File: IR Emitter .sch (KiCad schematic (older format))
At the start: 19 parts, among them U11 ULN2003APWR, U12 SMT_0540-S-R

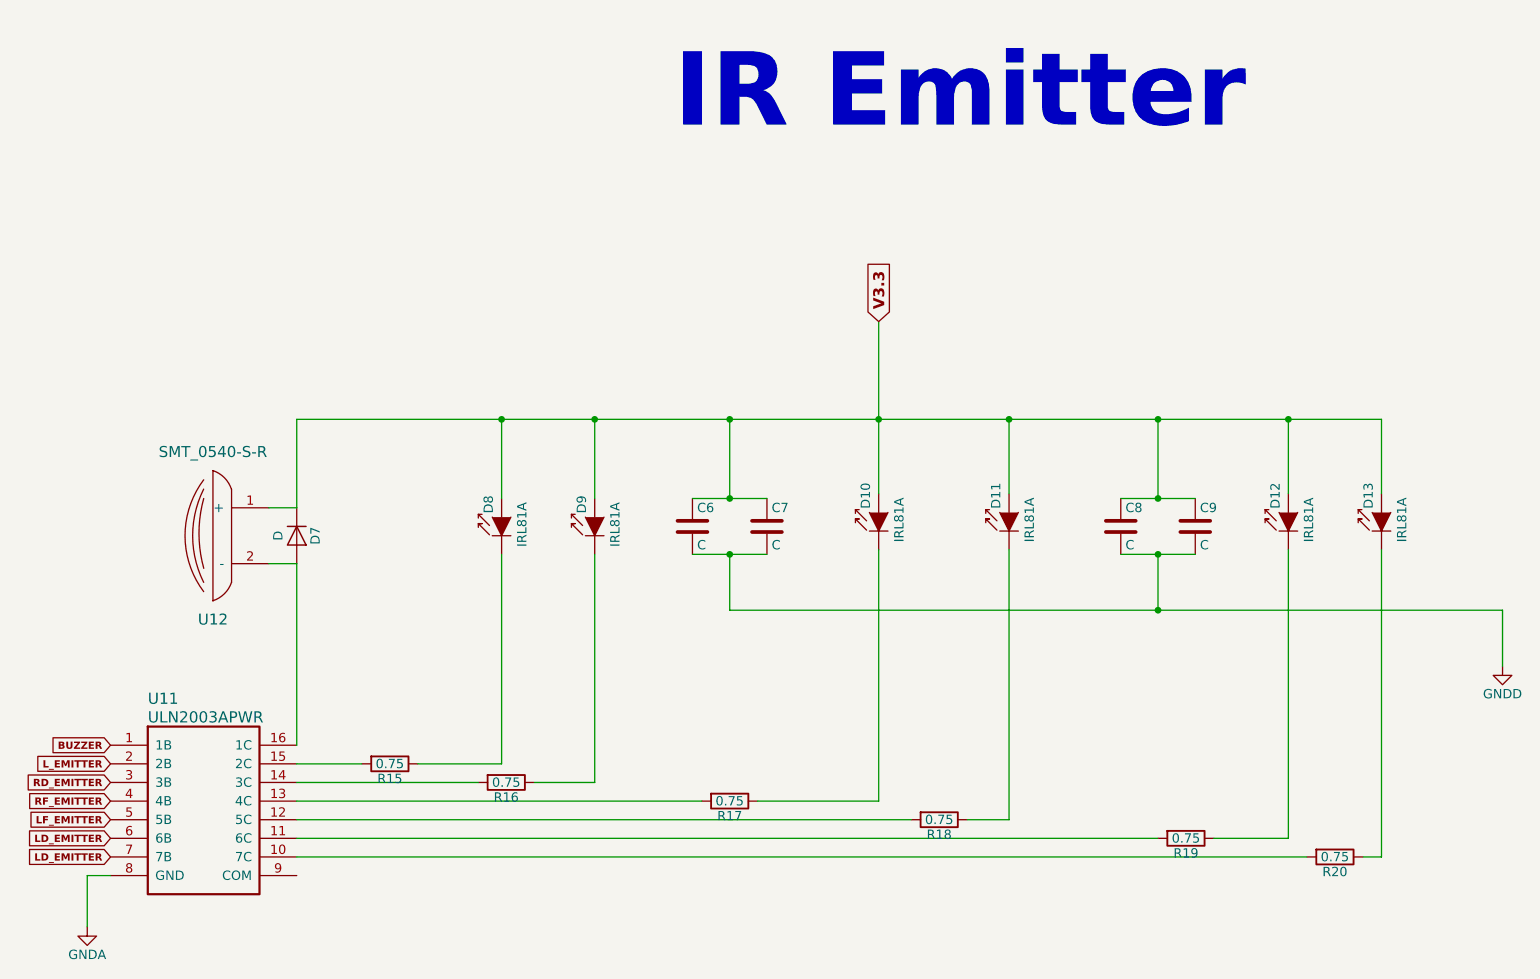
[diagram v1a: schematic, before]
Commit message: fixed the mergre conflicts from the adding datasheet commite
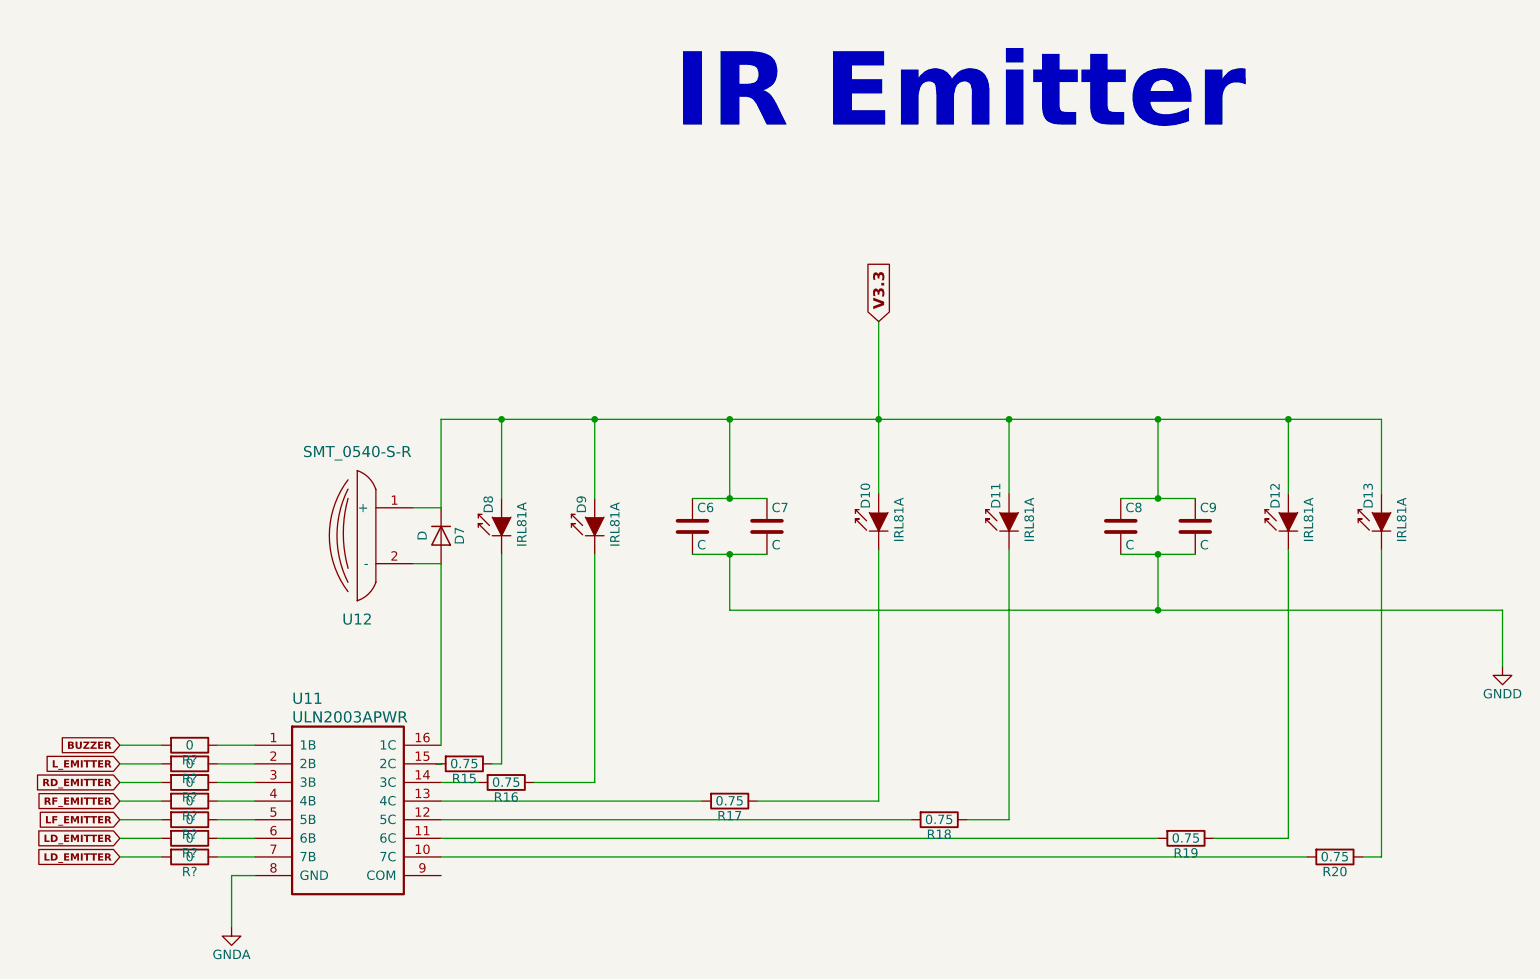
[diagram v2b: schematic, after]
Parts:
- added R? (x7): 0, symbol R
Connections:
- net BUZZER: now also R?.2; no longer U11.1 (1B)
- net LD_EMITTER: now also R?.2, R?.2; no longer U11.6 (6B), U11.7 (7B)
- net LF_EMITTER: now also R?.2; no longer U11.5 (5B)
- net L_EMITTER: now also R?.2; no longer U11.2 (2B)
- net RD_EMITTER: now also R?.2; no longer U11.3 (3B)
- net RF_EMITTER: now also R?.2; no longer U11.4 (4B)
- new net: R?.1, U11.1 (1B)
- new net: R?.1, U11.2 (2B)
- new net: R?.1, U11.3 (3B)
- new net: R?.1, U11.4 (4B)
- new net: R?.1, U11.5 (5B)
- new net: R?.1, U11.6 (6B)
- new net: R?.1, U11.7 (7B)
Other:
- moved on the sheet: D7, R15, U11, U12
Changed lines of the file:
@@
 L R R15
 U 1 1 594607AD
-P 2375 4775
-F 0 "R15" V 2455 4775 50  0000 C CNN
-F 1 "0.75" V 2375 4775 50  0000 C CNN
-F 2 "Resistors_SMD:R_0603" V 2305 4775 50  0001 C CNN
-F 3 "" H 2375 4775 50  0001 C CNN
-	1    2375 4775
+P 2775 4775
+F 0 "R15" V 2855 4775 50  0000 C CNN
+F 1 "0.75" V 2775 4775 50  0000 C CNN
+F 2 "Resistors_SMD:R_0603" V 2705 4775 50  0001 C CNN
+F 3 "" H 2775 4775 50  0001 C CNN
+	1    2775 4775
 	0    1    1    0
 $EndComp
@@
 	2975 3650 2975 4775
 Wire Wire Line
-	2975 4775 2525 4775
-Wire Wire Line
-	2225 4775 1875 4775
-Wire Wire Line
-	2850 4875 1875 4875
+	2975 4775 2925 4775
+Wire Wire Line
+	2625 4775 2650 4775
+Wire Wire Line
+	2850 4875 2650 4875
 Wire Wire Line
 	3150 4875 3475 4875
@@
 	6300 3650 6700 3650
 Wire Wire Line
-	4050 4975 1875 4975
+	4050 4975 2650 4975
 Wire Wire Line
 	5000 3625 5000 4975
@@
 	5000 4975 4350 4975
 Wire Wire Line
-	5175 5075 1875 5075
+	5175 5075 2650 5075
 Wire Wire Line
 	5700 3625 5700 5075
@@
 	5700 5075 5475 5075
 Wire Wire Line
-	6500 5175 1875 5175
+	6500 5175 2650 5175
 Wire Wire Line
 	6800 5175 7200 5175
@@
 	7200 5175 7200 3625
 Wire Wire Line
-	7300 5275 1875 5275
+	7300 5275 2650 5275
 Wire Wire Line
 	7700 3625 7700 5275
@@
 L ULN2003APWR U11
 U 1 1 59461B93
-P 875 4675
-F 0 "U11" H 1075 4925 60  0000 L CNN
-F 1 "ULN2003APWR" H 1075 4825 60  0000 L CNN
-F 2 "sop:TSSOP16" H 875 4675 60  0001 C CNN
-F 3 "" H 875 4675 60  0001 C CNN
-	1    875  4675
+P 1650 4675
+F 0 "U11" H 1850 4925 60  0000 L CNN
+F 1 "ULN2003APWR" H 1850 4825 60  0000 L CNN
+F 2 "sop:TSSOP16" H 1650 4675 60  0001 C CNN
+F 3 "" H 1650 4675 60  0001 C CNN
+	1    1650 4675
 	1    0    0    -1
 $EndComp
@@
 L SMT_0540-S-R U12
 U 1 1 59461CC9
-P 1425 3600
-F 0 "U12" H 1425 3200 59  0000 C CNN
-F 1 "SMT_0540-S-R" H 1425 4100 59  0000 C CNN
-F 2 "micromouse:Buzzer_SMT-0540-S-R" H 1425 3600 59  0001 C CNN
-F 3 "" H 1425 3600 59  0001 C CNN
-	1    1425 3600
-	1    0    0    -1
-$EndComp
-Wire Wire Line
-	1725 3700 1875 3700
-Wire Wire Line
-	1875 3700 1875 4675
+P 2200 3600
+F 0 "U12" H 2200 3200 59  0000 C CNN
+F 1 "SMT_0540-S-R" H 2200 4100 59  0000 C CNN
+F 2 "micromouse:Buzzer_SMT-0540-S-R" H 2200 3600 59  0001 C CNN
+F 3 "" H 2200 3600 59  0001 C CNN
+	1    2200 3600
+	1    0    0    -1
+$EndComp
+Wire Wire Line
+	2500 3700 2650 3700
+Wire Wire Line
+	2650 3700 2650 4675
 $Comp
 L GNDD #PWR08
@@
 $EndComp
 Wire Wire Line
-	8350 4250 8350 3950
-Wire Wire Line
-	8350 3950 4200 3950
+	8350 3950 8350 4250
+Wire Wire Line
+	4200 3950 8350 3950
 Wire Wire Line
 	4200 3950 4200 3650
@@
 	2975 3350 2975 2925
 Wire Wire Line
-	1875 2925 7700 2925
+	2650 2925 7700 2925
 Wire Wire Line
 	7700 2925 7700 3325
@@
 Connection ~ 6500 3350
 Wire Wire Line
-	1725 3400 1875 3400
-Wire Wire Line
-	1875 3400 1875 2925
+	2500 3400 2650 3400
+Wire Wire Line
+	2650 3400 2650 2925
 Connection ~ 2975 2925
 $Comp
 L D D7
 U 1 1 5946296D
-P 1875 3550
-F 0 "D7" H 1875 3650 50  0000 C CNN
-F 1 "D" H 1875 3450 50  0000 C CNN
-F 2 "Diodes_SMD:D_0603" H 1875 3550 50  0001 C CNN
-F 3 "" H 1875 3550 50  0001 C CNN
-	1    1875 3550
+P 2650 3550
+F 0 "D7" H 2650 3650 50  0000 C CNN
+F 1 "D" H 2650 3450 50  0000 C CNN
+F 2 "Diodes_SMD:D_0603" H 2650 3550 50  0001 C CNN
+F 3 "" H 2650 3550 50  0001 C CNN
+	1    2650 3550
 	0    1    1    0
 $EndComp
 Text GLabel 5000 2400 1    59   Input ~ 12
 V3.3
-Text GLabel 875  4775 0    39   Input ~ 8
+Text GLabel 925  4775 0    39   Input ~ 8
 L_EMITTER
-Text GLabel 875  4875 0    39   Input ~ 8
+Text GLabel 925  4875 0    39   Input ~ 8
 RD_EMITTER
-Text GLabel 875  4975 0    39   Input ~ 8
+Text GLabel 925  4975 0    39   Input ~ 8
 RF_EMITTER
-Text GLabel 875  5075 0    39   Input ~ 8
+Text GLabel 925  5075 0    39   Input ~ 8
 LF_EMITTER
-Text GLabel 875  4675 0    39   Input ~ 8
+Text GLabel 925  4675 0    39   Input ~ 8
 BUZZER
-Text GLabel 875  5175 0    39   Input ~ 8
+Text GLabel 925  5175 0    39   Input ~ 8
 LD_EMITTER
-Text GLabel 875  5275 0    39   Input ~ 8
+Text GLabel 925  5275 0    39   Input ~ 8
 LD_EMITTER
 $Comp
 L GNDA #PWR09
 U 1 1 59463543
-P 750 5650
-F 0 "#PWR09" H 750 5400 50  0001 C CNN
-F 1 "GNDA" H 750 5500 50  0000 C CNN
-F 2 "" H 750 5650 50  0001 C CNN
-F 3 "" H 750 5650 50  0001 C CNN
-	1    750  5650
-	1    0    0    -1
-$EndComp
-Wire Wire Line
-	750  5650 750  5375
-Wire Wire Line
-	750  5375 875  5375
+P 1525 5650
+F 0 "#PWR09" H 1525 5400 50  0001 C CNN
+F 1 "GNDA" H 1525 5500 50  0000 C CNN
+F 2 "" H 1525 5650 50  0001 C CNN
+F 3 "" H 1525 5650 50  0001 C CNN
+	1    1525 5650
+	1    0    0    -1
+$EndComp
+Wire Wire Line
+	1525 5650 1525 5375
+Wire Wire Line
+	1525 5375 1650 5375
 Text Notes 3900 1400 0    394  ~ 79
 IR Emitter
+$Comp
+L R R?
+U 1 1 5976EE2D
+P 1300 4675
+F 0 "R?" V 1380 4675 50  0000 C CNN
+F 1 "0" V 1300 4675 50  0000 C CNN
+F 2 "" V 1230 4675 50  0001 C CNN
+F 3 "" H 1300 4675 50  0001 C CNN
+	1    1300 4675
+	0    1    1    0
+$EndComp
+$Comp
+L R R?
+U 1 1 5976F354
+P 1300 4875
+F 0 "R?" V 1380 4875 50  0000 C CNN
+F 1 "0" V 1300 4875 50  0000 C CNN
+F 2 "" V 1230 4875 50  0001 C CNN
+F 3 "" H 1300 4875 50  0001 C CNN
+	1    1300 4875
+	0    1    1    0
+$EndComp
+$Comp
+L R R?
+U 1 1 5976F3DE
+P 1300 4775
+F 0 "R?" V 1380 4775 50  0000 C CNN
+F 1 "0" V 1300 4775 50  0000 C CNN
+F 2 "" V 1230 4775 50  0001 C CNN
+F 3 "" H 1300 4775 50  0001 C CNN
+	1    1300 4775
+	0    1    1    0
+$EndComp
+$Comp
+L R R?
+U 1 1 5976F49C
+P 1300 4975
+F 0 "R?" V 1380 4975 50  0000 C CNN
+F 1 "0" V 1300 4975 50  0000 C CNN
+F 2 "" V 1230 4975 50  0001 C CNN
+F 3 "" H 1300 4975 50  0001 C CNN
+	1    1300 4975
+	0    1    1    0
+$EndComp
+$Comp
+L R R?
+U 1 1 5976F4F7
+P 1300 5075
+F 0 "R?" V 1380 5075 50  0000 C CNN
+F 1 "0" V 1300 5075 50  0000 C CNN
+F 2 "" V 1230 5075 50  0001 C CNN
+F 3 "" H 1300 5075 50  0001 C CNN
+	1    1300 5075
+	0    1    1    0
+$EndComp
+$Comp
+L R R?
+U 1 1 5976F557
+P 1300 5175
+F 0 "R?" V 1380 5175 50  0000 C CNN
+F 1 "0" V 1300 5175 50  0000 C CNN
+F 2 "" V 1230 5175 50  0001 C CNN
+F 3 "" H 1300 5175 50  0001 C CNN
+	1    1300 5175
+	0    1    1    0
+$EndComp
+$Comp
+L R R?
+U 1 1 5976F840
+P 1300 5275
+F 0 "R?" V 1380 5275 50  0000 C CNN
+F 1 "0" V 1300 5275 50  0000 C CNN
+F 2 "" V 1230 5275 50  0001 C CNN
+F 3 "" H 1300 5275 50  0001 C CNN
+	1    1300 5275
+	0    1    1    0
+$EndComp
+Wire Wire Line
+	925  4675 1150 4675
+Wire Wire Line
+	1450 4675 1650 4675
+Wire Wire Line
+	1650 4775 1450 4775
+Wire Wire Line
+	1150 4775 925  4775
+Wire Wire Line
+	925  4875 1150 4875
+Wire Wire Line
+	1450 4875 1650 4875
+Wire Wire Line
+	1650 4975 1450 4975
+Wire Wire Line
+	1150 4975 925  4975
+Wire Wire Line
+	925  5075 1150 5075
+Wire Wire Line
+	1150 5175 925  5175
+Wire Wire Line
+	1150 5275 925  5275
+Wire Wire Line
+	1450 5275 1650 5275
+Wire Wire Line
+	1650 5175 1450 5175
+Wire Wire Line
+	1450 5075 1650 5075
 $EndSCHEMATC

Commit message: Added footprints for diode and both 16MHz and 32.678Mhz crystal
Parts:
- D11: footprint LEDs:LED_D5.0mm_Horizontal_O3.81mm_Z3.0mm -> micromouse:IR-Emitter
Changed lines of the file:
@@
 F 0 "D11" H 5720 3495 50  0000 L CNN
 F 1 "IRL81A" H 5660 3315 50  0000 C CNN
-F 2 "LEDs:LED_D5.0mm_Horizontal_O3.81mm_Z3.0mm" H 5700 3600 50  0001 C CNN
+F 2 "micromouse:IR-Emitter" H 5700 3600 50  0001 C CNN
 F 3 "" H 5650 3425 50  0000 C CNN
 	1    5700 3425
